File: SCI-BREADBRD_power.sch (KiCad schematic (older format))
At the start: 5 parts, among them SW1 DPDT, U1 SN74LVC1G08DBV

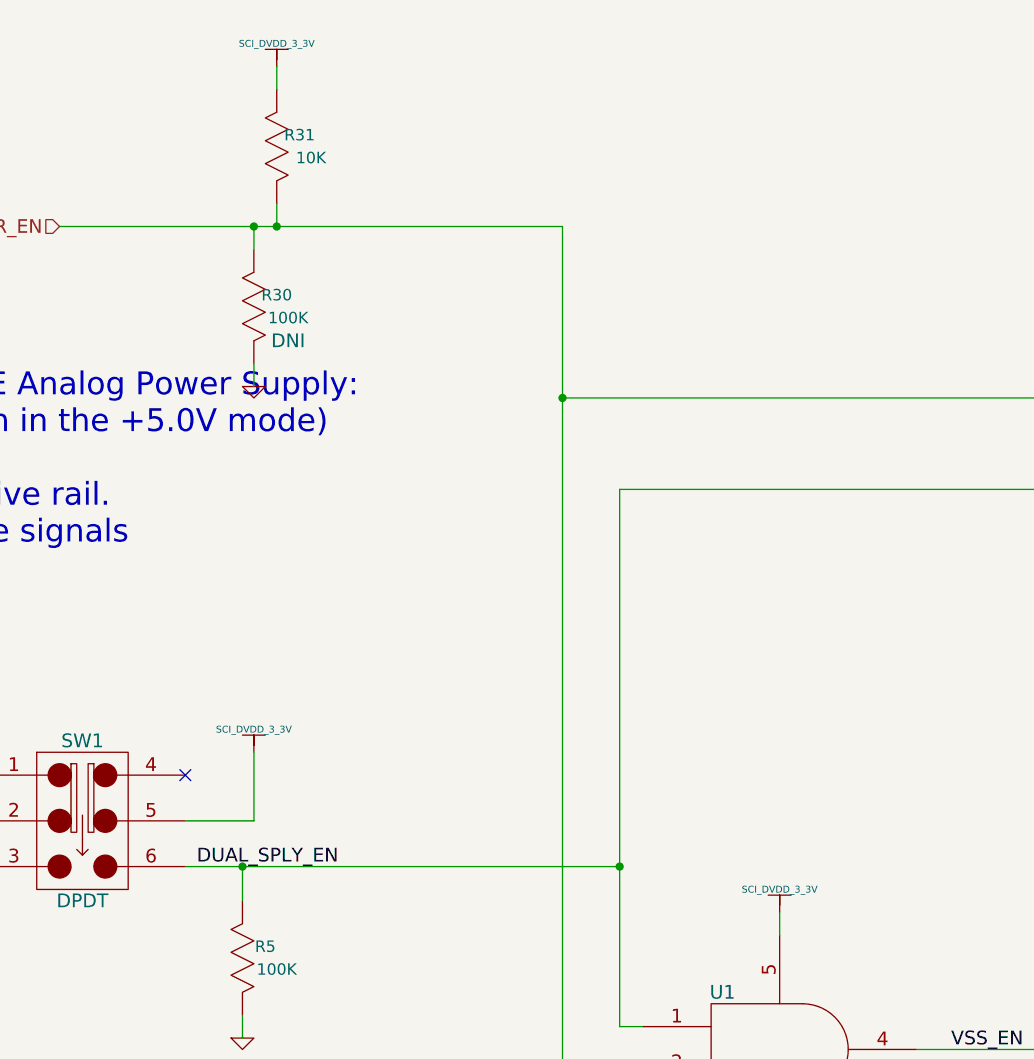
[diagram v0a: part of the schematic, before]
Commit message: Enlarged the text on all of the power rails to make them easier to see when plotted
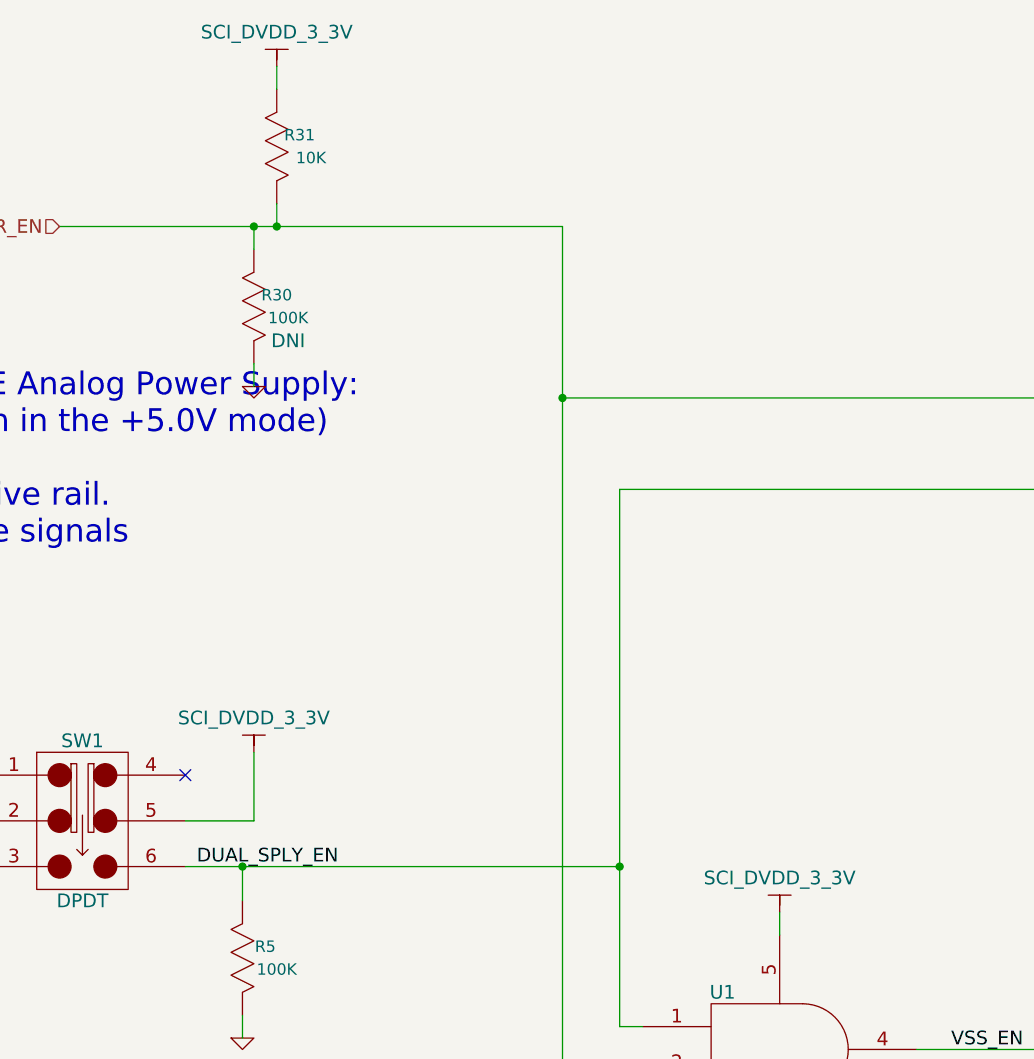
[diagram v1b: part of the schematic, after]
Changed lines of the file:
@@
-EESchema Schematic File Version 2  date Fri 27 Apr 2012 01:46:28 PM EDT
+EESchema Schematic File Version 2  date Fri 27 Apr 2012 02:46:40 PM EDT
 LIBS:custom_transistors
 LIBS:TI_custom
@@
 	1    0    0    -1
 $EndComp
-$Comp
-L SCI_DVDD_3_3V #PWR44
-U 1 1 4F9A18A3
-P 3650 4000
-F 0 "#PWR44" H 3650 4100 30  0001 C CNN
-F 1 "SCI_DVDD_3_3V" H 3650 4100 30  0000 C CNN
-	1    3650 4000
-	1    0    0    -1
-$EndComp
 NoConn ~ 3350 4100
 Text Label 3400 4500 0    60   ~ 0
 DUAL_SPLY_EN
-$Comp
-L SCI_DVDD_3_3V #PWR46
-U 1 1 4F9A1DFD
-P 5950 4700
-F 0 "#PWR46" H 5950 4800 30  0001 C CNN
-F 1 "SCI_DVDD_3_3V" H 5950 4800 30  0000 C CNN
-	1    5950 4700
-	1    0    0    -1
-$EndComp
 $Comp
 L GND #PWR47
@@
 	0    -1   -1   0
 $EndComp
-$Comp
-L SCI_DVDD_3_3V #PWR45
-U 1 1 4F9AB960
-P 3750 1000
-F 0 "#PWR45" H 3750 1100 30  0001 C CNN
-F 1 "SCI_DVDD_3_3V" H 3750 1100 30  0000 C CNN
-	1    3750 1000
-	1    0    0    -1
-$EndComp
 Wire Wire Line
 	1900 4400 1900 4300
@@
 	3350 4500 5250 4500
 Connection ~ 5250 4500
+$Comp
+L SCI_DVDD_3_3V #PWR?
+U 1 1 4F9AED7C
+P 3750 1000
+F 0 "#PWR?" H 3750 1100 30  0001 C CNN
+F 1 "SCI_DVDD_3_3V" H 3750 1150 60  0000 C CNN
+	1    3750 1000
+	1    0    0    -1
+$EndComp
+$Comp
+L SCI_DVDD_3_3V #PWR?
+U 1 1 4F9AEECF
+P 3650 4000
+F 0 "#PWR?" H 3650 4100 30  0001 C CNN
+F 1 "SCI_DVDD_3_3V" H 3650 4150 60  0000 C CNN
+	1    3650 4000
+	1    0    0    -1
+$EndComp
+$Comp
+L SCI_DVDD_3_3V #PWR?
+U 1 1 4F9AEF3E
+P 5950 4700
+F 0 "#PWR?" H 5950 4800 30  0001 C CNN
+F 1 "SCI_DVDD_3_3V" H 5950 4850 60  0000 C CNN
+	1    5950 4700
+	1    0    0    -1
+$EndComp
 $EndSCHEMATC

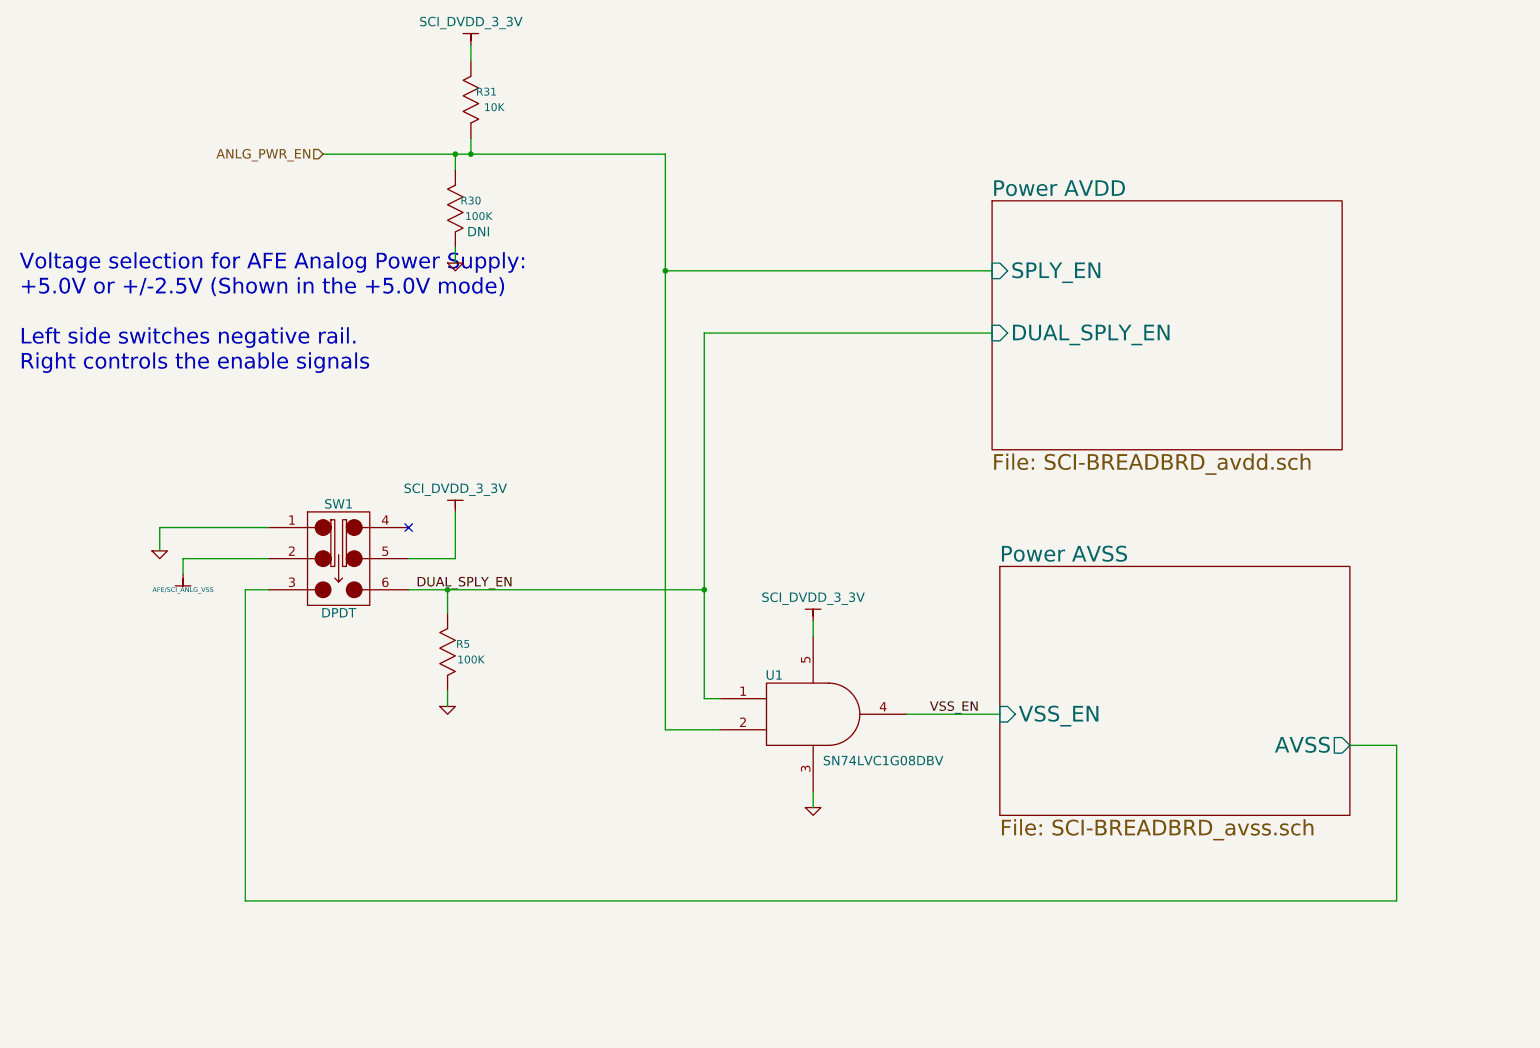
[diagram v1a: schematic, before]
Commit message: No longer connecting the power circuitry directly to AFE/SCI_ANLG power rails.
This is just too dangerous with AFE modules that also generate power
on those rails. For this board, the user can manually jumper the
circuitry to the rails as desired.
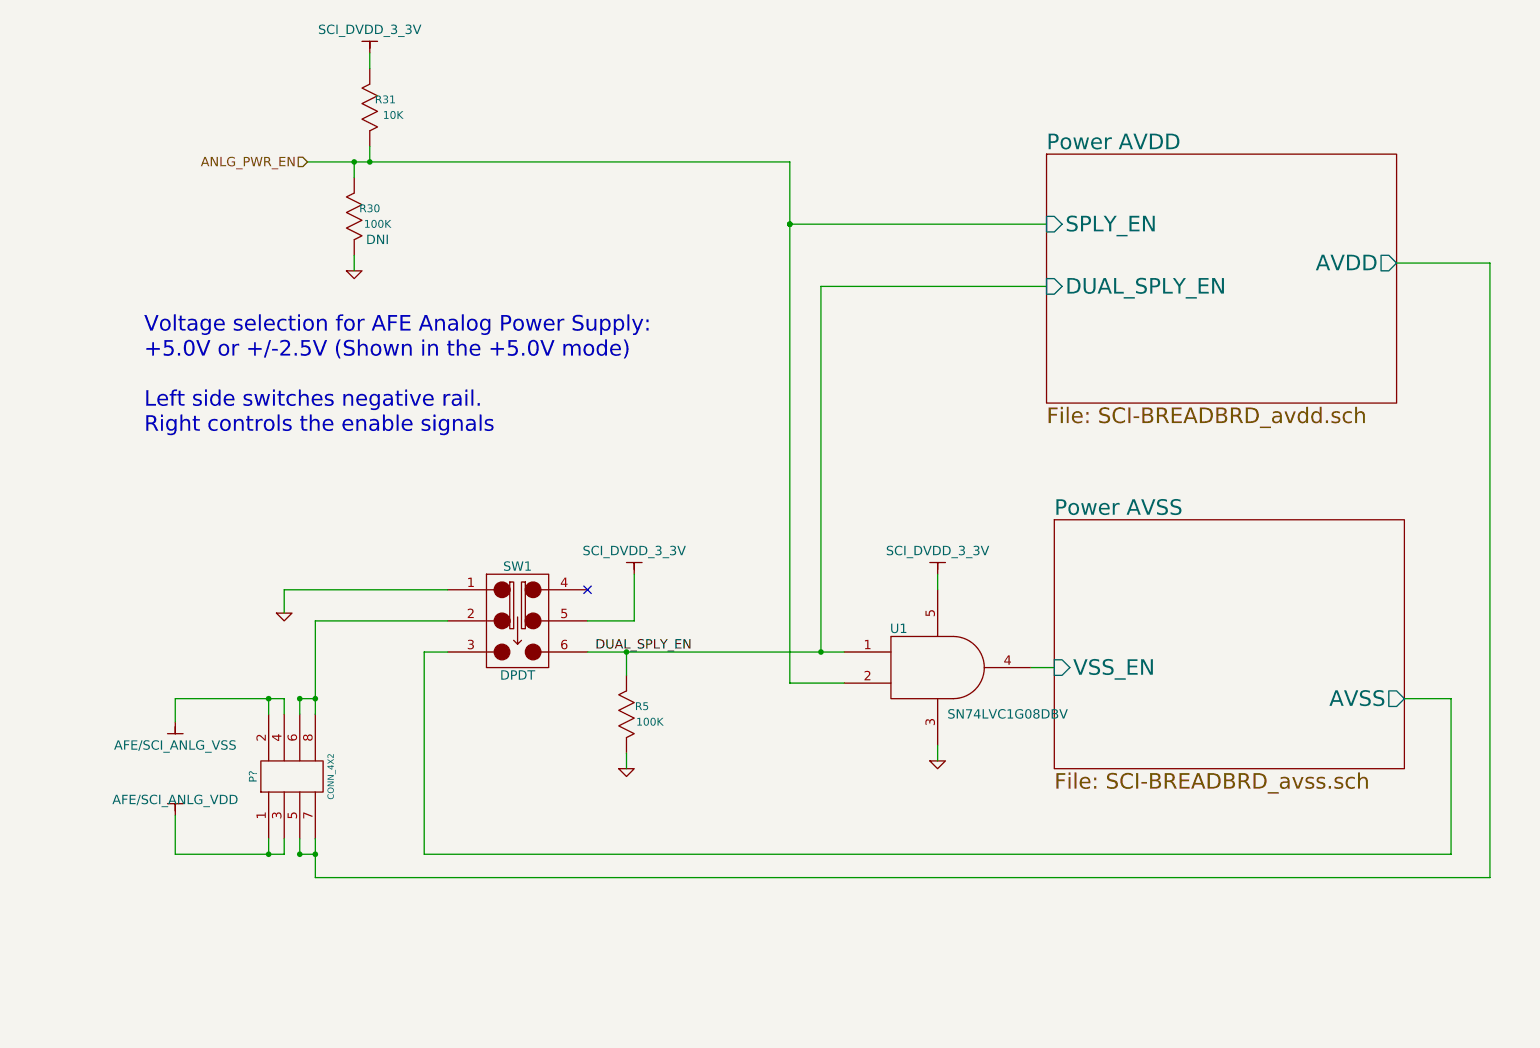
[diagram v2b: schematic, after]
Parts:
- added P?: CONN_4X2, pin_array_4x2, symbol CONN_4X2
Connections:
- net AFE/SCI_ANLG_VSS: now also P?.2, P?.4; no longer SW1.2
- net VSS_EN renamed Power AVSS/VSS_EN
- new net: P?.6, P?.8, SW1.2
- new net AFE/SCI_ANLG_VDD: P?.1, P?.3
- new net Power AVDD/AVDD: P?.5, P?.7
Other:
- moved on the sheet: R30, R31, R5, SW1, U1

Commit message: Re-annotated for added parts.
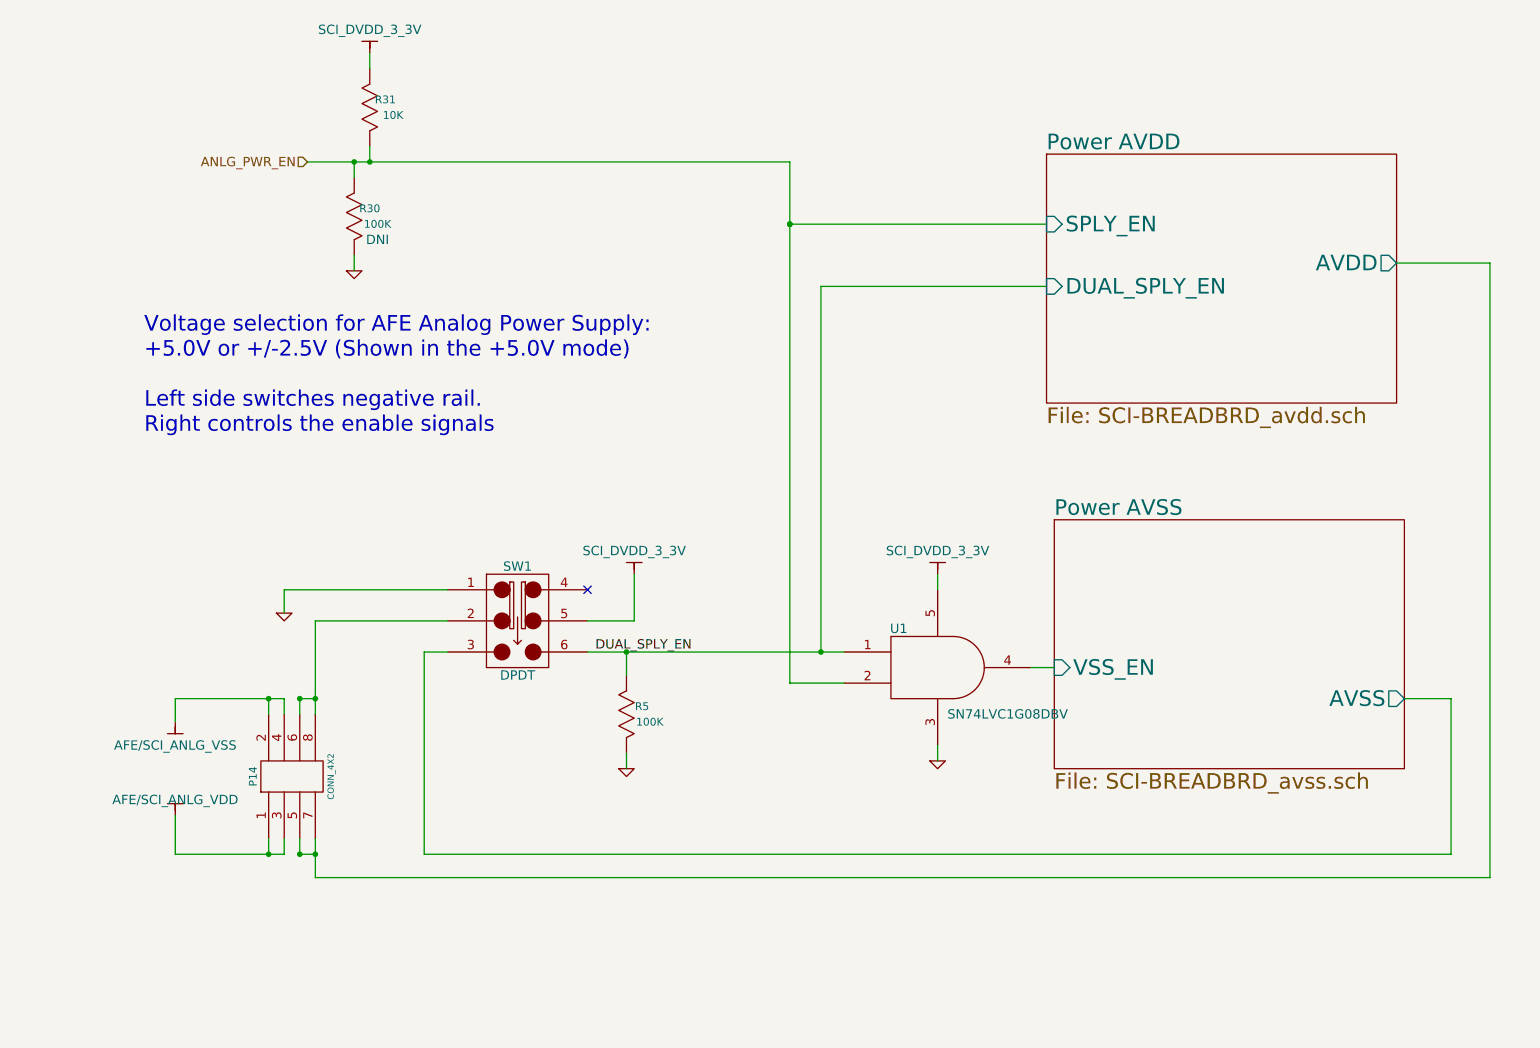
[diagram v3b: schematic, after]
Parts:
- gave numbers to parts that had none: 1
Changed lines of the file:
@@
-EESchema Schematic File Version 2  date Tue 01 May 2012 11:50:09 PM EDT
+EESchema Schematic File Version 2  date Wed 02 May 2012 02:37:03 AM EDT
 LIBS:custom_transistors
 LIBS:TI_custom
@@
 $EndComp
 $Comp
-L GND #PWR40
+L GND #PWR042
 U 1 1 4F9A1627
 P 2550 4650
-F 0 "#PWR40" H 2550 4650 30  0001 C CNN
+F 0 "#PWR042" H 2550 4650 30  0001 C CNN
 F 1 "GND" H 2550 4580 30  0001 C CNN
 	1    2550 4650
@@
 DUAL_SPLY_EN
 $Comp
-L GND #PWR47
+L GND #PWR043
 U 1 1 4F9A1F73
 P 6750 5600
-F 0 "#PWR47" H 6750 5600 30  0001 C CNN
+F 0 "#PWR043" H 6750 5600 30  0001 C CNN
 F 1 "GND" H 6750 5530 30  0001 C CNN
 	1    6750 5600
@@
 $EndComp
 $Comp
-L GND #PWR42
+L GND #PWR044
 U 1 1 4F9A4A85
 P 4750 5650
-F 0 "#PWR42" H 4750 5650 30  0001 C CNN
+F 0 "#PWR044" H 4750 5650 30  0001 C CNN
 F 1 "GND" H 4750 5580 30  0001 C CNN
 	1    4750 5650
@@
 $EndComp
 $Comp
-L GND #PWR43
+L GND #PWR045
 U 1 1 4F9AB470
 P 3000 2450
-F 0 "#PWR43" H 3000 2450 30  0001 C CNN
+F 0 "#PWR045" H 3000 2450 30  0001 C CNN
 F 1 "GND" H 3000 2380 30  0001 C CNN
 	1    3000 2450
@@
 $EndComp
 $Comp
-L SCI_DVDD_3_3V #PWR?
+L SCI_DVDD_3_3V #PWR046
 U 1 1 4F9AED7C
 P 3100 1050
-F 0 "#PWR?" H 3100 1150 30  0001 C CNN
+F 0 "#PWR046" H 3100 1150 30  0001 C CNN
 F 1 "SCI_DVDD_3_3V" H 3100 1200 60  0000 C CNN
 	1    3100 1050
@@
 $EndComp
 $Comp
-L SCI_DVDD_3_3V #PWR?
+L SCI_DVDD_3_3V #PWR047
 U 1 1 4F9AEECF
 P 4800 4400
-F 0 "#PWR?" H 4800 4500 30  0001 C CNN
+F 0 "#PWR047" H 4800 4500 30  0001 C CNN
 F 1 "SCI_DVDD_3_3V" H 4800 4550 60  0000 C CNN
 	1    4800 4400
@@
 $EndComp
 $Comp
-L SCI_DVDD_3_3V #PWR?
+L SCI_DVDD_3_3V #PWR048
 U 1 1 4F9AEF3E
 P 6750 4400
-F 0 "#PWR?" H 6750 4500 30  0001 C CNN
+F 0 "#PWR048" H 6750 4500 30  0001 C CNN
 F 1 "SCI_DVDD_3_3V" H 6750 4550 60  0000 C CNN
 	1    6750 4400
@@
 $EndComp
 $Comp
-L AFE/SCI_ANLG_VSS #PWR?
+L AFE/SCI_ANLG_VSS #PWR049
 U 1 1 4FA0D213
 P 1850 5350
-F 0 "#PWR?" H 1850 5250 30  0001 C CNN
+F 0 "#PWR049" H 1850 5250 30  0001 C CNN
 F 1 "AFE/SCI_ANLG_VSS" H 1850 5200 60  0000 C CNN
 	1    1850 5350
@@
 $EndComp
 $Comp
-L CONN_4X2 P?
+L CONN_4X2 P14
 U 1 1 4FA0D66E
 P 2600 5700
-F 0 "P?" H 2600 5950 50  0000 C CNN
+F 0 "P14" H 2600 5950 50  0000 C CNN
 F 1 "CONN_4X2" H 2600 5450 40  0000 C CNN
 F 2 "pin_array_4x2" H 2600 5700 60  0001 C CNN
@@
 $EndComp
 $Comp
-L AFE/SCI_ANLG_VDD #PWR?
+L AFE/SCI_ANLG_VDD #PWR050
 U 1 1 4FA0E56B
 P 1850 5950
-F 0 "#PWR?" H 1850 6050 30  0001 C CNN
+F 0 "#PWR050" H 1850 6050 30  0001 C CNN
 F 1 "AFE/SCI_ANLG_VDD" H 1850 6050 60  0000 C CNN
 	1    1850 5950
@@
 $EndComp
 Wire Wire Line
-	2750 4700 2750 5200
-Wire Wire Line
-	2750 5200 2750 5300
+	2750 4700 2750 5300
 Wire Wire Line
 	2750 4700 3600 4700
@@
 	7350 5000 7500 5000
 Wire Wire Line
-	4500 4900 4750 4900
-Wire Wire Line
-	4750 4900 6000 4900
-Wire Wire Line
-	6000 4900 6150 4900
+	4500 4900 6150 4900
 Wire Wire Line
 	9750 5200 10050 5200
@@
 	6000 2550 7450 2550
 Wire Wire Line
-	2700 1750 3000 1750
-Wire Wire Line
-	3000 1750 3100 1750
-Wire Wire Line
-	3100 1750 5800 1750
+	2700 1750 5800 1750
 Wire Wire Line
 	5800 5100 6150 5100
@@
 	3100 1050 3100 1150
 Wire Wire Line
-	5800 1750 5800 2150
-Wire Wire Line
-	5800 2150 5800 5100
+	5800 1750 5800 5100
 Connection ~ 5800 2150
 Wire Wire Line
@@
 	2650 6200 2650 6100
 Wire Wire Line
-	2750 6100 2750 6200
-Wire Wire Line
-	2750 6200 2750 6350
+	2750 6100 2750 6350
 Connection ~ 2650 6200
 Connection ~ 2750 6200
@@
 	1850 5350 1850 5200
 Wire Wire Line
-	1850 5200 2450 5200
-Wire Wire Line
-	2450 5200 2550 5200
+	1850 5200 2550 5200
 Wire Wire Line
 	2550 5200 2550 5300
@@
 	1850 5950 1850 6200
 Wire Wire Line
-	1850 6200 2450 6200
-Wire Wire Line
-	2450 6200 2550 6200
+	1850 6200 2550 6200
 Wire Wire Line
 	2550 6200 2550 6100
